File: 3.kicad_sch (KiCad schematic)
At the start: 21 parts, among them IC1 LMR14010A, IC2 LMR14010A

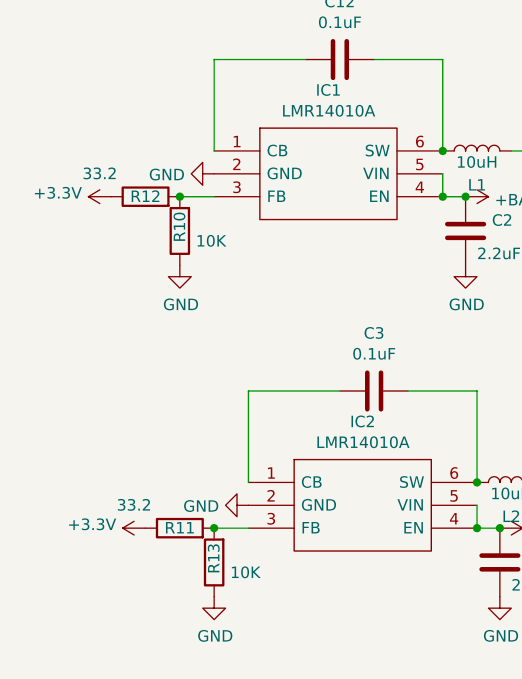
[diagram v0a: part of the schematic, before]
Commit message: Addressing the issues with the sample version, Updating the bom to source all the correct components from the JLCPCB supply
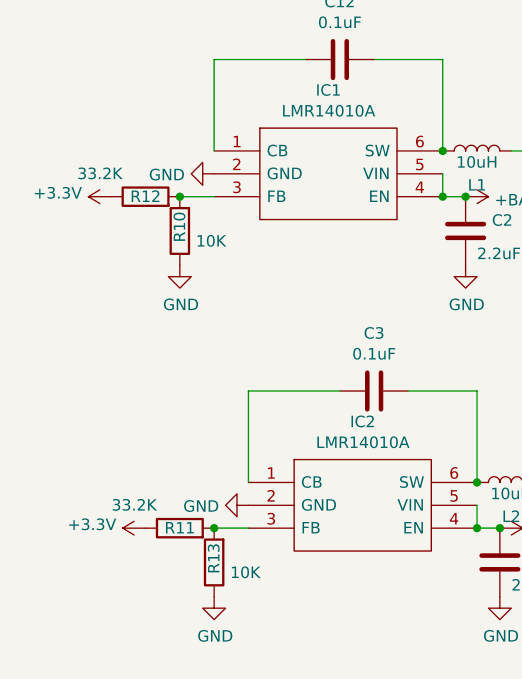
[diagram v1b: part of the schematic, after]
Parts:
- R11, R12: value 33.2 -> 33.2K
- TP4: now left out of the parts list
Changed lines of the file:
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@@
     (in_bom yes) (on_board yes)
     (property "Reference" "R12" (id 0) (at 132.08 36.83 90))
-    (property "Value" "33.2" (id 1) (at 127 34.29 90))
+    (property "Value" "33.2K" (id 1) (at 127 34.29 90))
     (property "Footprint" "Resistor_SMD:R_0402_1005Metric" (id 2) (at 132.08 38.608 90)
       (effects (font (size 1.27 1.27)) hide)
@@
   )
   (symbol (lib_id "Connector:TestPoint") (at 232.41 105.41 0) (unit 1)
-    (in_bom yes) (on_board yes)
+    (in_bom no) (on_board yes)
     (property "Reference" "TP4" (id 0) (at 233.8832 102.4128 0)
       (effects (font (size 1.27 1.27)) (justify left))
@@
     (in_bom yes) (on_board yes)
     (property "Reference" "R11" (id 0) (at 135.89 73.66 90))
-    (property "Value" "33.2" (id 1) (at 130.81 71.12 90))
+    (property "Value" "33.2K" (id 1) (at 130.81 71.12 90))
     (property "Footprint" "Resistor_SMD:R_0402_1005Metric" (id 2) (at 135.89 75.438 90)
       (effects (font (size 1.27 1.27)) hide)

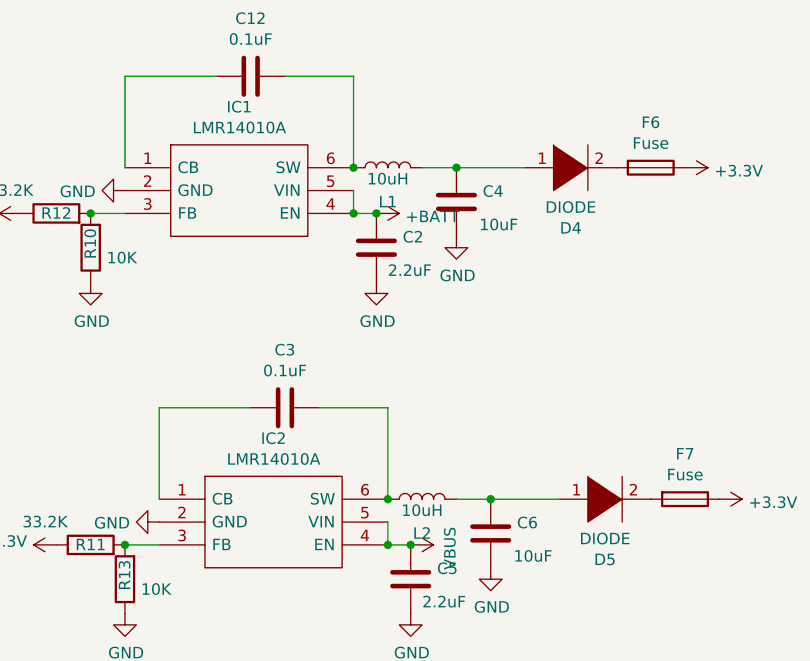
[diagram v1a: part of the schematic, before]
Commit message: Adding usb c pd negotiation for battery charging
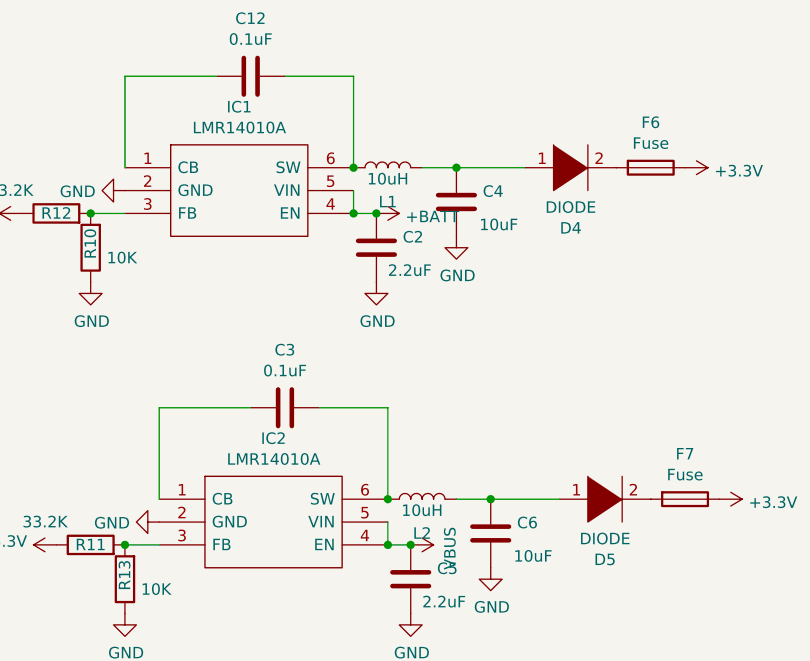
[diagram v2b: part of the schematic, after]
